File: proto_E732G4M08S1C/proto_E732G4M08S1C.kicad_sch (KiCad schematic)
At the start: 0 parts

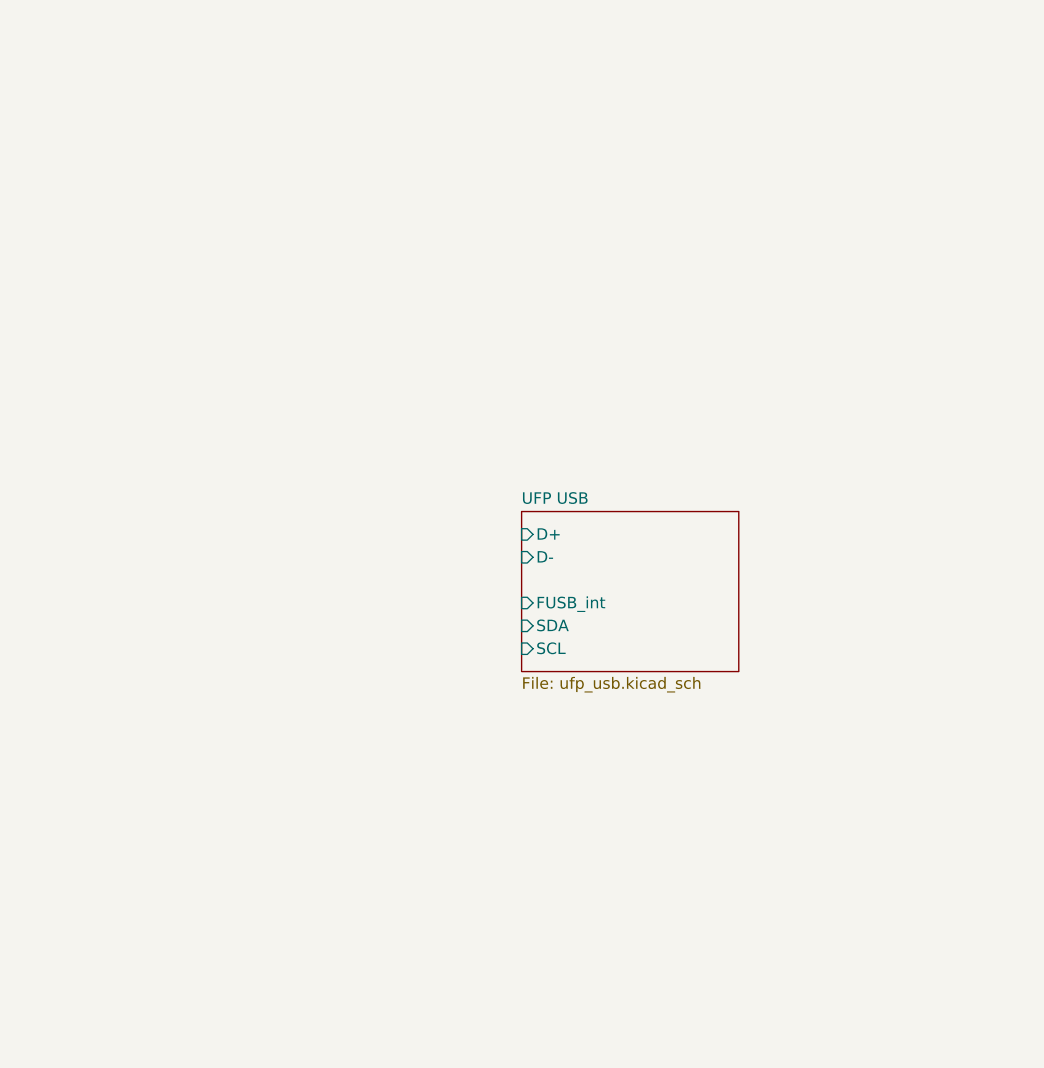
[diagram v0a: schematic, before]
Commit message: feat(pcb) initial blocks and MCU
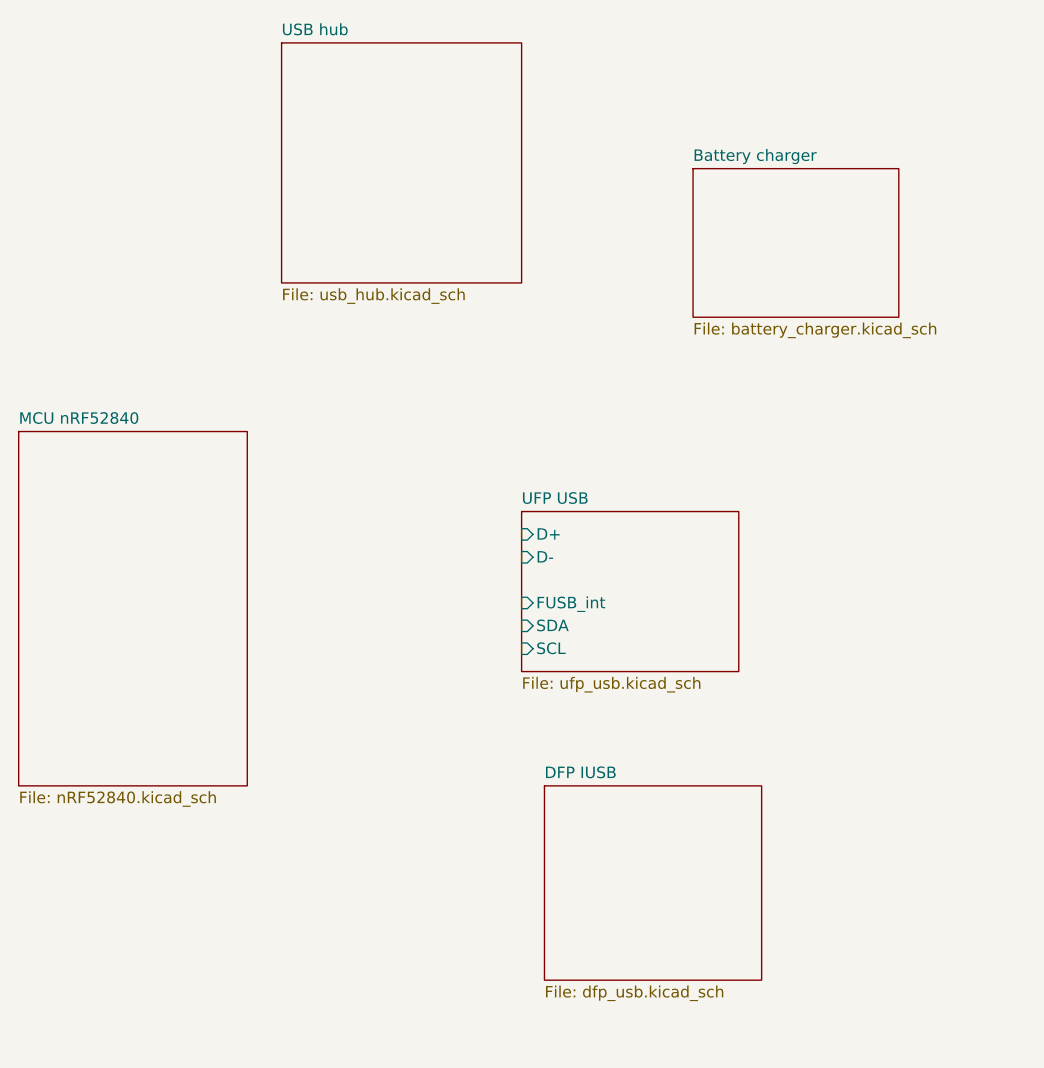
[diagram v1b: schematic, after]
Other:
- added sheet Battery charger (battery_charger.kicad_sch)
- added sheet DFP IUSB (dfp_usb.kicad_sch)
- added sheet MCU nRF52840 (nRF52840.kicad_sch)
- added sheet USB hub (usb_hub.kicad_sch)
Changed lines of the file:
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@@
+	)
+	(sheet
+		(at 175.26 29.21)
+		(size 26.67 26.67)
+		(exclude_from_sim no)
+		(in_bom yes)
+		(on_board yes)
+		(dnp no)
+		(fields_autoplaced yes)
+		(stroke
+			(width 0.1524)
+			(type solid)
+		)
+		(fill
+			(color 0 255 255 1.0000)
+		)
+		(property "Sheetname" "USB hub"
+			(at 175.26 28.4984 0)
+			(effects
+				(font
+					(size 1.27 1.27)
+				)
+				(justify left bottom)
+			)
+		)
+		(property "Sheetfile" "usb_hub.kicad_sch"
+			(at 175.26 56.4646 0)
+			(effects
+				(font
+					(size 1.27 1.27)
+				)
+				(justify left top)
+			)
+		)
+		(instances
+			(project "proto_E732G4M08S1C"
+				(path "/3062eac5-ad35-4bd4-9fe0-12754d69cac0"
+					(page "6")
+				)
+			)
+		)
+	)
+	(sheet
+		(at 146.05 72.39)
+		(size 25.4 39.37)
+		(exclude_from_sim no)
+		(in_bom yes)
+		(on_board yes)
+		(dnp no)
+		(fields_autoplaced yes)
+		(stroke
+			(width 0.1524)
+			(type solid)
+		)
+		(fill
+			(color 0 255 255 1.0000)
+		)
+		(property "Sheetname" "MCU nRF52840"
+			(at 146.05 71.6784 0)
+			(effects
+				(font
+					(size 1.27 1.27)
+				)
+				(justify left bottom)
+			)
+		)
+		(property "Sheetfile" "nRF52840.kicad_sch"
+			(at 146.05 112.3446 0)
+			(effects
+				(font
+					(size 1.27 1.27)
+				)
+				(justify left top)
+			)
+		)
+		(instances
+			(project "proto_E732G4M08S1C"
+				(path "/3062eac5-ad35-4bd4-9fe0-12754d69cac0"
+					(page "3")
+				)
+			)
+		)
+	)
+	(sheet
+		(at 220.98 43.18)
+		(size 22.86 16.51)
+		(exclude_from_sim no)
+		(in_bom yes)
+		(on_board yes)
+		(dnp no)
+		(fields_autoplaced yes)
+		(stroke
+			(width 0.1524)
+			(type solid)
+		)
+		(fill
+			(color 0 255 255 1.0000)
+		)
+		(property "Sheetname" "Battery charger"
+			(at 220.98 42.4684 0)
+			(effects
+				(font
+					(size 1.27 1.27)
+				)
+				(justify left bottom)
+			)
+		)
+		(property "Sheetfile" "battery_charger.kicad_sch"
+			(at 220.98 60.2746 0)
+			(effects
+				(font
+					(size 1.27 1.27)
+				)
+				(justify left top)
+			)
+		)
+		(instances
+			(project "proto_E732G4M08S1C"
+				(path "/3062eac5-ad35-4bd4-9fe0-12754d69cac0"
+					(page "4")
+				)
+			)
+		)
 	)
 	(sheet
@@
 		)
 		(fill
-			(color 0 194 194 1.0000)
+			(color 0 255 255 1.0000)
 		)
 		(property "Sheetname" "UFP USB"
@@
 				)
 			)
+		)
+	)
+	(sheet
+		(at 204.47 111.76)
+		(size 24.13 21.59)
+		(exclude_from_sim no)
+		(in_bom yes)
+		(on_board yes)
+		(dnp no)
+		(fields_autoplaced yes)
+		(stroke
+			(width 0.1524)
+			(type solid)
+		)
+		(fill
+			(color 0 255 255 1.0000)
+		)
+		(property "Sheetname" "DFP IUSB"
+			(at 204.47 111.0484 0)
+			(effects
+				(font
+					(size 1.27 1.27)
+				)
+				(justify left bottom)
+			)
+		)
+		(property "Sheetfile" "dfp_usb.kicad_sch"
+			(at 204.47 133.9346 0)
+			(effects
+				(font
+					(size 1.27 1.27)
+				)
+				(justify left top)
+			)
+		)
+		(instances
+			(project "proto_E732G4M08S1C"
+				(path "/3062eac5-ad35-4bd4-9fe0-12754d69cac0"
+					(page "5")
+				)
+			)

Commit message: feat(pcb) more changes
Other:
- sheet Battery charger ports: added Imax_en1, Imax_en2; removed none
- sheet DFP IUSB ports: added D+, D-, FUSB_int, SCL, SDA, UART_rx, UART_tx, serial_enable; removed none
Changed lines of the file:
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@@
 	(sheet
 		(at 220.98 43.18)
-		(size 22.86 16.51)
+		(size 22.86 7.62)
 		(exclude_from_sim no)
 		(in_bom yes)
@@
 		)
 		(property "Sheetfile" "battery_charger.kicad_sch"
-			(at 220.98 60.2746 0)
+			(at 220.98 51.3846 0)
 			(effects
 				(font
@@
 				)
 				(justify left top)
+			)
+		)
+		(pin "Imax_en2" input
+			(at 220.98 48.26 180)
+			(effects
+				(font
+					(size 1.27 1.27)
+				)
+				(justify left)
+			)
+		)
+		(pin "Imax_en1" input
+			(at 220.98 45.72 180)
+			(effects
+				(font
+					(size 1.27 1.27)
+				)
+				(justify left)
 			)
 		)
@@
 	(sheet
 		(at 204.47 111.76)
-		(size 24.13 21.59)
+		(size 24.13 26.67)
 		(exclude_from_sim no)
 		(in_bom yes)
@@
 		)
 		(property "Sheetfile" "dfp_usb.kicad_sch"
-			(at 204.47 133.9346 0)
+			(at 204.47 139.0146 0)
 			(effects
 				(font
@@
 			)
 		)
+		(pin "UART_rx" input
+			(at 204.47 133.35 180)
+			(effects
+				(font
+					(size 1.27 1.27)
+				)
+				(justify left)
+			)
+		)
+		(pin "FUSB_int" input
+			(at 204.47 127 180)
+			(effects
+				(font
+					(size 1.27 1.27)
+				)
+				(justify left)
+			)
+		)
+		(pin "SCL" input
+			(at 204.47 124.46 180)
+			(effects
+				(font
+					(size 1.27 1.27)
+				)
+				(justify left)
+			)
+		)
+		(pin "D-" input
+			(at 204.47 116.84 180)
+			(effects
+				(font
+					(size 1.27 1.27)
+				)
+				(justify left)
+			)
+		)
+		(pin "D+" input
+			(at 204.47 114.3 180)
+			(effects
+				(font
+					(size 1.27 1.27)
+				)
+				(justify left)
+			)
+		)
+		(pin "SDA" input
+			(at 204.47 121.92 180)
+			(effects
+				(font
+					(size 1.27 1.27)
+				)
+				(justify left)
+			)
+		)
+		(pin "UART_tx" output
+			(at 204.47 135.89 180)
+			(effects
+				(font
+					(size 1.27 1.27)
+				)
+				(justify left)
+			)
+		)
+		(pin "serial_enable" input
+			(at 204.47 130.81 180)
+			(effects
+				(font
+					(size 1.27 1.27)
+				)
+				(justify left)
+			)
+		)
